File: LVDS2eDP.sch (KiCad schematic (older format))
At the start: 60 parts, among them U301 IT6251, X301 27MHz 50ppm, 8-18pF, ESR < 80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

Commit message: Schematic notes
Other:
- note added: "LVDS to eDP Converter"
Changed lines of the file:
@@
 Wire Wire Line
 	5050 6400 5050 6500
+Text Notes 4750 800  0    157  ~ 0
+LVDS to eDP Converter
 $EndSCHEMATC

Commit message: Initial footprint association, last few footprints
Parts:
- C301, C302, C303, C305, C306, C307, C309, C310, C311, C313, C314, C316, C317, C318, C319, C320: value 100nF 25V X54 -> 100nF 25V X5R; footprint (none) -> SMD_Packages:SMD-0402_c
- C304, C308, C312: value 1nF 25V X54 -> 1nF 25V X5R; footprint (none) -> SMD_Packages:SMD-0402_c
- C315: value 1uF 25V X54 -> 1uF 25V X5R; footprint (none) -> SMD_Packages:SMD-0402_c
- C321, C322, R312, R313, R314, R315, R316, R317, R318, R319: footprint (none) -> FT:0603
- C323, C324, C325, C326, C327, C328, C329, C330, C331, C332, C333: footprint (none) -> SMD_Packages:SMD-0402_c
- R301, R302, R303, R304, R305, R306, R307, R308, R309, R310, R311: footprint (none) -> SMD_Packages:SMD-0402_r
- TP301, TP302, TP303, TP304, TP305, TP306: footprint (none) -> novepad:SMD_TEST_POINT
- U301: footprint (none) -> novepad:QFN50P900X900X100-65N
- X301: footprint (none) -> FT:HC49UP

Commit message: Super-zealous length matching version
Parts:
- removed C307, C316, C319, C320: 100nF 25V X5R, SMD_Packages:SMD-0402_c, symbol C
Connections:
- net GND is gone; now on net +1.8VA: C301.2, C302.2, C303.2, C304.2, C305.2, C306.2, C308.2, C309.2, C310.2, C311.2, C312.2, C313.2, C314.2, C315.2, C317.2, C318.2, C321.2, C322.2, C323.2, R314.2, R319.2, U301.PAD (GND)
- net +1.8V: no longer C302.1, C304.1, C306.1, C308.1, C309.1, C310.1, C311.1, C312.1, C313.1, C314.1
- net +1.8VA: now also C302.1, C304.1, C306.1, C308.1, C309.1, C310.1, C311.1, C312.1, C313.1, C314.1
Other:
- note added: "Decoupling pins 26,41,49,52"
- note added: "Decoupling pins 6,11,46"
- note removed: "Decoupling pins 6,11,21,26,41,46,49,52"
- moved on the sheet: C309, C311, C313, C314, C315, C317, C318

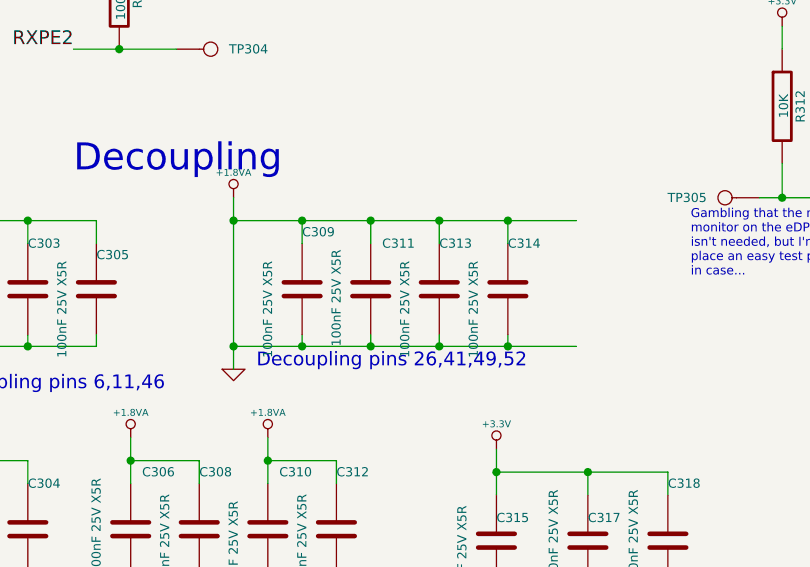
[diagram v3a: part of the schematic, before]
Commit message: Routed, passes DRC
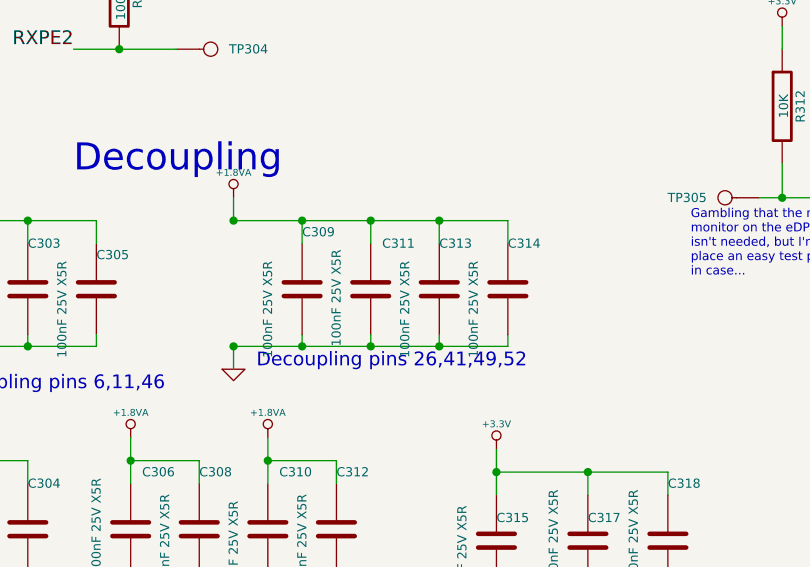
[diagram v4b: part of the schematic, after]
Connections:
- net +1.8VA: no longer C301.2, C302.2, C303.2, C304.2, C305.2, C306.2, C308.2, C309.2, C310.2, C311.2, C312.2, C313.2, C314.2, C315.2, C317.2, C318.2, C321.2, C322.2, C323.2, R314.2, R319.2, U301.PAD (GND)
- new net GND: C301.2, C302.2, C303.2, C304.2, C305.2, C306.2, C308.2, C309.2, C310.2, C311.2, C312.2, C313.2, C314.2, C315.2, C317.2, C318.2, C321.2, C322.2, C323.2, R314.2, R319.2, U301.PAD (GND)

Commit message: More cleanup
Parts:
- added TP307, TP308, TP309: CONN_1, novepad:SMD_TEST_POINT, symbol CONN_1
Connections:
- net +1.8V: no longer C323.1, R316.1
- net +1.8VA: now also C323.1, R316.1
- net at U301.10 (DBG2): now also TP309.1
- net at U301.8 (DBG0): now also TP307.1
- net at U301.9 (DBG1): now also TP308.1
- no-connect marks 3 -> 0
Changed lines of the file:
@@
 $EndComp
 $Comp
-L GND #PWR020
+L GND #PWR318
 U 1 1 5441389E
 P 5550 6950
-F 0 "#PWR020" H 5550 6950 30  0001 C CNN
+F 0 "#PWR318" H 5550 6950 30  0001 C CNN
 F 1 "GND" H 5550 6880 30  0001 C CNN
 F 2 "" H 5550 6950 60  0000 C CNN
@@
 $EndComp
 $Comp
-L GND #PWR021
+L GND #PWR320
 U 1 1 544138D3
 P 6150 6950
-F 0 "#PWR021" H 6150 6950 30  0001 C CNN
+F 0 "#PWR320" H 6150 6950 30  0001 C CNN
 F 1 "GND" H 6150 6880 30  0001 C CNN
 F 2 "" H 6150 6950 60  0000 C CNN
@@
 $EndComp
 $Comp
-L GND #PWR022
+L GND #PWR321
 U 1 1 54413D0B
 P 7200 5150
-F 0 "#PWR022" H 7200 5150 30  0001 C CNN
+F 0 "#PWR321" H 7200 5150 30  0001 C CNN
 F 1 "GND" H 7200 5080 30  0001 C CNN
 F 2 "" H 7200 5150 60  0000 C CNN
@@
 	1    0    0    -1
 $EndComp
-NoConn ~ 6250 5000
-NoConn ~ 6350 5000
-NoConn ~ 6450 5000
 $Comp
 L IT6251 U301
@@
 $EndComp
 $Comp
-L GND #PWR023
+L GND #PWR325
 U 1 1 544156AF
 P 10350 2050
-F 0 "#PWR023" H 10350 2050 30  0001 C CNN
+F 0 "#PWR325" H 10350 2050 30  0001 C CNN
 F 1 "GND" H 10350 1980 30  0001 C CNN
 F 2 "" H 10350 2050 60  0000 C CNN
@@
 $EndComp
 $Comp
-L GND #PWR024
+L GND #PWR316
 U 1 1 54415DFB
 P 5050 7650
-F 0 "#PWR024" H 5050 7650 30  0001 C CNN
+F 0 "#PWR316" H 5050 7650 30  0001 C CNN
 F 1 "GND" H 5050 7580 30  0001 C CNN
 F 2 "" H 5050 7650 60  0000 C CNN
@@
 $EndComp
 $Comp
-L +3.3V #PWR025
+L +3.3V #PWR313
 U 1 1 54416493
 P 4400 4950
-F 0 "#PWR025" H 4400 4910 30  0001 C CNN
+F 0 "#PWR313" H 4400 4910 30  0001 C CNN
 F 1 "+3.3V" H 4400 5060 30  0000 C CNN
 F 2 "" H 4400 4950 60  0000 C CNN
@@
 $EndComp
 $Comp
-L +3.3V #PWR026
+L +3.3V #PWR314
 U 1 1 5448BB6B
 P 4550 1300
-F 0 "#PWR026" H 4550 1260 30  0001 C CNN
+F 0 "#PWR314" H 4550 1260 30  0001 C CNN
 F 1 "+3.3V" H 4550 1410 30  0000 C CNN
 F 2 "" H 4550 1300 60  0000 C CNN
@@
 $EndComp
 $Comp
-L +1.8V #PWR027
+L +1.8V #PWR317
 U 1 1 5448BF6C
 P 5150 1300
-F 0 "#PWR027" H 5150 1440 20  0001 C CNN
+F 0 "#PWR317" H 5150 1440 20  0001 C CNN
 F 1 "+1.8V" H 5150 1410 30  0000 C CNN
 F 2 "" H 5150 1300 60  0000 C CNN
@@
 $EndComp
 $Comp
-L +3.3V #PWR028
+L +3.3V #PWR311
 U 1 1 5448E7F9
 P 3150 6800
-F 0 "#PWR028" H 3150 6760 30  0001 C CNN
+F 0 "#PWR311" H 3150 6760 30  0001 C CNN
 F 1 "+3.3V" H 3150 6910 30  0000 C CNN
 F 2 "" H 3150 6800 60  0000 C CNN
@@
 $EndComp
 $Comp
-L GND #PWR029
+L GND #PWR312
 U 1 1 5448EF58
 P 3150 7550
-F 0 "#PWR029" H 3150 7550 30  0001 C CNN
+F 0 "#PWR312" H 3150 7550 30  0001 C CNN
 F 1 "GND" H 3150 7480 30  0001 C CNN
 F 2 "" H 3150 7550 60  0000 C CNN
 F 3 "" H 3150 7550 60  0000 C CNN
 	1    3150 7550
-	1    0    0    -1
-$EndComp
-$Comp
-L +1.8V #PWR030
-U 1 1 54490A24
-P 9250 5550
-F 0 "#PWR030" H 9250 5690 20  0001 C CNN
-F 1 "+1.8V" H 9250 5660 30  0000 C CNN
-F 2 "" H 9250 5550 60  0000 C CNN
-F 3 "" H 9250 5550 60  0000 C CNN
-	1    9250 5550
 	1    0    0    -1
 $EndComp
@@
 $EndComp
 $Comp
-L GND #PWR031
+L GND #PWR323
 U 1 1 54490D49
 P 9250 6200
-F 0 "#PWR031" H 9250 6200 30  0001 C CNN
+F 0 "#PWR323" H 9250 6200 30  0001 C CNN
 F 1 "GND" H 9250 6130 30  0001 C CNN
 F 2 "" H 9250 6200 60  0000 C CNN
@@
 $EndComp
 $Comp
-L GND #PWR032
+L GND #PWR302
 U 1 1 54495582
 P 800 6450
-F 0 "#PWR032" H 800 6450 30  0001 C CNN
+F 0 "#PWR302" H 800 6450 30  0001 C CNN
 F 1 "GND" H 800 6380 30  0001 C CNN
 F 2 "" H 800 6450 60  0000 C CNN
@@
 $EndComp
 $Comp
-L +1.8V #PWR033
+L +1.8V #PWR301
 U 1 1 54495E5D
 P 800 5700
-F 0 "#PWR033" H 800 5840 20  0001 C CNN
+F 0 "#PWR301" H 800 5840 20  0001 C CNN
 F 1 "+1.8V" H 800 5810 30  0000 C CNN
 F 2 "" H 800 5700 60  0000 C CNN
@@
 Near pin 4
 $Comp
-L GND #PWR034
+L GND #PWR304
 U 1 1 54498187
 P 800 7500
-F 0 "#PWR034" H 800 7500 30  0001 C CNN
+F 0 "#PWR304" H 800 7500 30  0001 C CNN
 F 1 "GND" H 800 7430 30  0001 C CNN
 F 2 "" H 800 7500 60  0000 C CNN
@@
 $EndComp
 $Comp
-L GND #PWR035
+L GND #PWR306
 U 1 1 54498B12
 P 1550 7500
-F 0 "#PWR035" H 1550 7500 30  0001 C CNN
+F 0 "#PWR306" H 1550 7500 30  0001 C CNN
 F 1 "GND" H 1550 7430 30  0001 C CNN
 F 2 "" H 1550 7500 60  0000 C CNN
@@
 $EndComp
 $Comp
-L GND #PWR036
+L GND #PWR310
 U 1 1 5449A5CB
 P 2150 7500
-F 0 "#PWR036" H 2150 7500 30  0001 C CNN
+F 0 "#PWR310" H 2150 7500 30  0001 C CNN
 F 1 "GND" H 2150 7430 30  0001 C CNN
 F 2 "" H 2150 7500 60  0000 C CNN
@@
 $EndComp
 $Comp
-L +3.3V #PWR037
+L +3.3V #PWR324
 U 1 1 544A93F6
 P 10350 650
-F 0 "#PWR037" H 10350 610 30  0001 C CNN
+F 0 "#PWR324" H 10350 610 30  0001 C CNN
 F 1 "+3.3V" H 10350 760 30  0000 C CNN
 F 2 "" H 10350 650 60  0000 C CNN
@@
 $EndComp
 $Comp
-L +3.3V #PWR038
+L +3.3V #PWR315
 U 1 1 544ECA5F
 P 5050 6400
-F 0 "#PWR038" H 5050 6360 30  0001 C CNN
+F 0 "#PWR315" H 5050 6360 30  0001 C CNN
 F 1 "+3.3V" H 5050 6510 30  0000 C CNN
 F 2 "" H 5050 6400 60  0000 C CNN
@@
 Decoupling pins 6,11,46
 $Comp
-L GND #PWR039
+L GND #PWR308
 U 1 1 5469DEF4
 P 2000 6450
-F 0 "#PWR039" H 2000 6450 30  0001 C CNN
+F 0 "#PWR308" H 2000 6450 30  0001 C CNN
 F 1 "GND" H 2000 6380 30  0001 C CNN
 F 2 "" H 2000 6450 60  0000 C CNN
@@
 $EndComp
 $Comp
-L +1.8VA #PWR040
+L +1.8VA #PWR309
 U 1 1 54783EA4
 P 2150 6750
-F 0 "#PWR040" H 2150 6890 20  0001 C CNN
+F 0 "#PWR309" H 2150 6890 20  0001 C CNN
 F 1 "+1.8VA" H 2150 6860 30  0000 C CNN
 F 2 "" H 2150 6750 60  0000 C CNN
@@
 $EndComp
 $Comp
-L +1.8VA #PWR041
+L +1.8VA #PWR305
 U 1 1 547847B7
 P 1550 6750
-F 0 "#PWR041" H 1550 6890 20  0001 C CNN
+F 0 "#PWR305" H 1550 6890 20  0001 C CNN
 F 1 "+1.8VA" H 1550 6860 30  0000 C CNN
 F 2 "" H 1550 6750 60  0000 C CNN
@@
 $EndComp
 $Comp
-L +1.8VA #PWR042
+L +1.8VA #PWR303
 U 1 1 54784832
 P 800 6750
-F 0 "#PWR042" H 800 6890 20  0001 C CNN
+F 0 "#PWR303" H 800 6890 20  0001 C CNN
 F 1 "+1.8VA" H 800 6860 30  0000 C CNN
 F 2 "" H 800 6750 60  0000 C CNN
@@
 $EndComp
 $Comp
-L +1.8VA #PWR043
+L +1.8VA #PWR319
 U 1 1 54785227
 P 5700 1300
-F 0 "#PWR043" H 5700 1440 20  0001 C CNN
+F 0 "#PWR319" H 5700 1440 20  0001 C CNN
 F 1 "+1.8VA" H 5700 1410 30  0000 C CNN
 F 2 "" H 5700 1300 60  0000 C CNN
@@
 $EndComp
 $Comp
-L +1.8VA #PWR044
+L +1.8VA #PWR307
 U 1 1 5478629E
 P 2000 5700
-F 0 "#PWR044" H 2000 5840 20  0001 C CNN
+F 0 "#PWR307" H 2000 5840 20  0001 C CNN
 F 1 "+1.8VA" H 2000 5810 30  0000 C CNN
 F 2 "" H 2000 5700 60  0000 C CNN
@@
 Wire Wire Line
 	3200 5800 2000 5800
+$Comp
+L +1.8VA #PWR322
+U 1 1 547B9DD1
+P 9250 5550
+F 0 "#PWR322" H 9250 5690 20  0001 C CNN
+F 1 "+1.8VA" H 9250 5660 30  0000 C CNN
+F 2 "" H 9250 5550 60  0000 C CNN
+F 3 "" H 9250 5550 60  0000 C CNN
+	1    9250 5550
+	1    0    0    -1
+$EndComp
+$Comp
+L CONN_1 TP309
+U 1 1 547BAD69
+P 6600 5100
+F 0 "TP309" H 6680 5100 40  0000 L CNN
+F 1 "CONN_1" H 6600 5155 30  0001 C CNN
+F 2 "novepad:SMD_TEST_POINT" H 6600 5100 60  0001 C CNN
+F 3 "" H 6600 5100 60  0000 C CNN
+	1    6600 5100
+	1    0    0    -1
+$EndComp
+$Comp
+L CONN_1 TP308
+U 1 1 547BAE81
+P 6500 5200
+F 0 "TP308" H 6580 5200 40  0000 L CNN
+F 1 "CONN_1" H 6500 5255 30  0001 C CNN
+F 2 "novepad:SMD_TEST_POINT" H 6500 5200 60  0001 C CNN
+F 3 "" H 6500 5200 60  0000 C CNN
+	1    6500 5200
+	1    0    0    -1
+$EndComp
+$Comp
+L CONN_1 TP307
+U 1 1 547BAED9
+P 6400 5300
+F 0 "TP307" H 6480 5300 40  0000 L CNN
+F 1 "CONN_1" H 6400 5355 30  0001 C CNN
+F 2 "novepad:SMD_TEST_POINT" H 6400 5300 60  0001 C CNN
+F 3 "" H 6400 5300 60  0000 C CNN
+	1    6400 5300
+	1    0    0    -1
+$EndComp
+Wire Wire Line
+	6250 5300 6250 5000
+Wire Wire Line
+	6350 5200 6350 5000
+Wire Wire Line
+	6450 5100 6450 5000
 $EndSCHEMATC
